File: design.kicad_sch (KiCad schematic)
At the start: 1 part

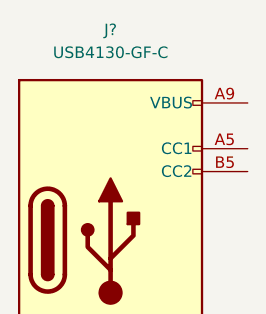
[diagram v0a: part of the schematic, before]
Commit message: annotate + usb connector 3D
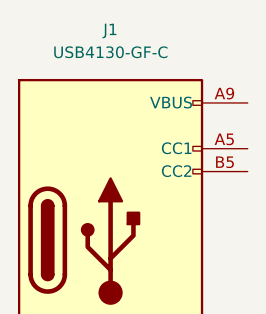
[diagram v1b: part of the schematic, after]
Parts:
- gave numbers to parts that had none: 1
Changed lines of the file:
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@@
   (symbol (lib_id "Connector_custom:USB4130-GF-C") (at 69.088 65.278 0) (unit 1)
     (in_bom yes) (on_board yes) (fields_autoplaced)
-    (property "Reference" "J?" (id 0) (at 69.088 41.91 0))
+    (property "Reference" "J1" (id 0) (at 69.088 41.91 0))
     (property "Value" "USB4130-GF-C" (id 1) (at 69.088 44.45 0))
     (property "Footprint" "Connector_USB_custom:USB_C_Receptacle_GCT_USB4130-GF-C" (id 2) (at 72.898 65.278 0)
@@
   (symbol_instances
     (path "/b1b78902-1557-46e9-9466-76f6cf11f8e2"
-      (reference "J?") (unit 1) (value "USB4130-GF-C") (footprint "Connector_USB_custom:USB_C_Receptacle_GCT_USB4130-GF-C")
+      (reference "J1") (unit 1) (value "USB4130-GF-C") (footprint "Connector_USB_custom:USB_C_Receptacle_GCT_USB4130-GF-C")
     )
   )

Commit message: update template to v0.45
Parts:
- added C?: 100nF, Capacitor_SMD:C_0805_2012Metric, symbol Device:C_Small
- added C?: 10uF, Capacitor_SMD:C_0805_2012Metric, symbol Device:C_Small
- added C?: 0-50pF, Capacitor_SMD:C_0805_2012Metric, symbol Device:C_Small
- added C? (x3): 1uF, Capacitor_SMD:C_0805_2012Metric, symbol Device:C_Small
- added C?: 0.1uF, Capacitor_SMD:C_0805_2012Metric, symbol Device:C_Small
- added D?: D_Small, Diode_SMD:D_SOD-323, symbol Device:D_Small
- added D?: LED, LED_SMD:LED_0603_1608Metric, symbol Device:LED
- added JP?: TOG, Jumper:SolderJumper-2_P1.3mm_Open_RoundedPad1.0x1.5mm, symbol Jumper:Jumper_2_Open
- added JP?: AHLB, Jumper:SolderJumper-2_P1.3mm_Open_RoundedPad1.0x1.5mm, symbol Jumper:Jumper_2_Open
- added R? (x5): 10K, Resistor_SMD:R_0805_2012Metric, symbol Device:R_Small
- added R?: 470, Resistor_SMD:R_0805_2012Metric, symbol Device:R_Small
- added SW?: EN, Button_Switch_SMD:SW_SPST_EVPBF, symbol Switch:SW_Push
- added SW?: IO9, Button_Switch_SMD:SW_SPST_EVPBF, symbol Switch:SW_Push
- added TP? (x3): Vin, TestPoint:TestPoint_Pad_D2.5mm, symbol Connector:TestPoint
- added TP?: touch_point_1, symbol Connector:TestPoint
- added TP?: +3.3V, TestPoint:TestPoint_Pad_D2.5mm, symbol Connector:TestPoint
- added TP?: Vbat, TestPoint:TestPoint_Pad_D2.5mm, symbol Connector:TestPoint
- added TP?: GND, TestPoint:TestPoint_Pad_D2.5mm, symbol Connector:TestPoint
- added U?: TCK108AF,LF, Package_TO_SOT_SMD:SOT-23-5, symbol Power_Management_custom:TCK108AF,LF
- added U?: ESP32-C3-WROOM-02-N4, MCU_Espressif_custom:MODULE_ESP32-C3-WROOM-02-H4, symbol MCU_Espressif_custom:ESP32-C3-WROOM-02-N4
- added U?: TTP223, Package_TO_SOT_SMD:SOT-23-6_Handsoldering, symbol LEDs:TTP223
- added U?: MCP1700-3302E_SOT23, Package_TO_SOT_SMD:SOT-23, symbol Regulator_Linear:MCP1700-3302E_SOT23
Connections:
- new net: C?.1, U?.2 (VO), U?.5 (VIN)
- new net: JP?.1 (A), U?.6 (TOG)
- new net: D?.1 (K), R?.1
- new net +3.3V: C?.1, C?.1, R?.1, R?.1, R?.1, R?.1, TP?.1, U?.1 (3V3), U?.1 (VOUT)
- new net +5V: C?.1, U?.3 (VI)
- new net D+: TP?.1, U?.14 (IO19)
- new net D-: TP?.1, U?.13 (IO18)
- new net EN: C?.1, R?.2, SW?.2, U?.2 (EN)
- new net GND: C?.2, C?.2, C?.2, C?.2, C?.2, C?.2, C?.2, R?.2, R?.2, SW?.1, SW?.1, TP?.1, U?.1 (GND), U?.19 (GND), U?.2 (GND), U?.2 (GND), U?.20 (GND), U?.21 (GND), U?.22 (GND), U?.23 (GND), U?.24 (GND), U?.25 (GND), U?.26 (GND), U?.27 (GND), U?.28 (GND), U?.29 (GND), U?.30 (GND), U?.31 (GND), U?.32 (GND), U?.33 (GND), U?.34 (GND), U?.35 (GND), U?.36 (GND), U?.37 (GND), U?.38 (GND), U?.39 (GND), U?.9 (GND)
- new net IO0: U?.18 (IO0)
- new net IO1: U?.17 (IO1)
- new net IO10: U?.10 (IO10)
- new net IO2: R?.2, U?.16 (IO2)
- new net IO3: U?.15 (IO3)
- new net IO4: U?.3 (IO4)
- new net IO5: D?.2 (A), U?.1 (Q), U?.4 (IO5)
- new net IO6: D?.1 (K), R?.1, U?.3 (Control), U?.5 (IO6)
- new net IO7: D?.2 (A), U?.6 (IO7)
- new net IO8: R?.2, U?.7 (IO8)
- new net IO9: R?.2, SW?.2, U?.8 (IO9)
- new net MCU_RX: U?.11 (RXD)
- new net MCU_TX: U?.12 (TXD)
- new net VCC: C?.1, JP?.2 (B), U?.5 (VCC)
- new net Vbat: TP?.1
- new net Vin: TP?.1
- new net touch_point_1: C?.1, TP?.1, U?.3 (I)
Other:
- note added: "No intenal LDO - feed with fixed valtage between 2-5.5V"
- note added: "TOG: LOW - Direct Mode HIGH - Toggle Mode AHLB: LOW - CMOS active high output HIGH - CMOS active low output"
- note added: "Touch"
- note added: "Touch IC TTP223"
- moved on the sheet: J1

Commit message: Update design.kicad_sch
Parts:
- removed D?: D_Small, Diode_SMD:D_SOD-323, symbol Device:D_Small
- removed JP?: AHLB, Jumper:SolderJumper-2_P1.3mm_Open_RoundedPad1.0x1.5mm, symbol Jumper:Jumper_2_Open
- added JP?: AHLB, symbol Jumper:Jumper_2_Bridged
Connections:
- net IO5: no longer U?.1 (Q)
- net IO6: now also U?.1 (Q)
- net VCC: now also JP?.2 (B)
- net at U?.4 (AHLB): now also JP?.1 (A)
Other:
- moved on the sheet: C?, D?, JP?, R?, SW?, TP?, U?

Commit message: PCB&SCH update
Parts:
- removed TP?: Vin, TestPoint:TestPoint_Pad_D2.5mm, symbol Connector:TestPoint
- removed TP?: Vbat, TestPoint:TestPoint_Pad_D2.5mm, symbol Connector:TestPoint
- added R7, R8: 5.1k, Resistor_SMD:R_0805_2012Metric, symbol Device:R_Small
- added TP4: +BATT, TestPoint:TestPoint_Pad_D2.5mm, symbol Connector:TestPoint
- JP2: renamed from JP?; footprint (none) -> Jumper:SolderJumper-2_P1.3mm_Open_RoundedPad1.0x1.5mm
- TP2: renamed from TP?; value Vin -> D-
- TP3: renamed from TP?; value Vin -> D+
- gave numbers to parts that had none: 24
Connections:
- net VCC is gone; now on net +BATT: C6.1, JP1.2 (B), JP2.2 (B), U4.5 (VCC)
- net +3.3V: now also C2.1, U1.2 (VO); no longer U2.1 (VOUT)
- net GND: now also J1.A12 (GND), J1.B12 (GND), R7.2, R8.2
- net at J1.A5 (CC1): now also R7.1
- net +BATT: now reaches J1.A9 (VBUS), J1.B9 (VBUS)
- net +BATT: now also U2.5 (VIN), TP4.1
- net at J1.B5 (CC2): now also R8.1
- net +5V: no longer names the net of C1.1, U1.3 (VI)
- net +5V: now also U2.1 (VOUT)
- no-connect marks 0 -> 1
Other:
- moved on the sheet: C1, C2, R1, TP5, U1, U2A

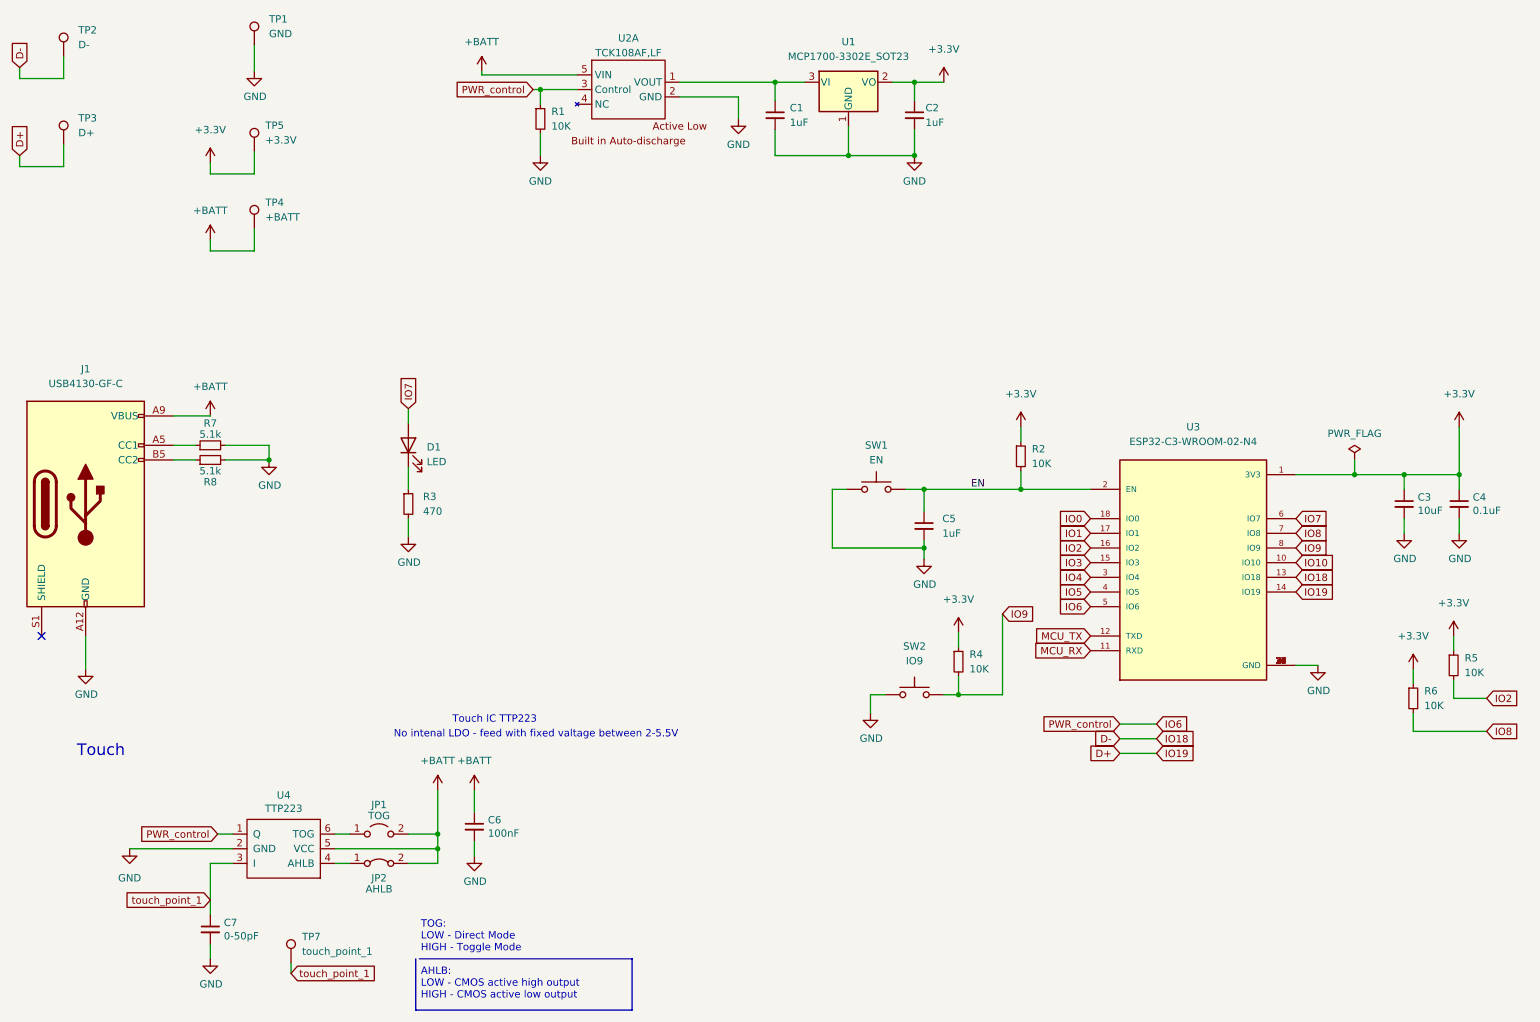
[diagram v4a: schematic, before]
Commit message: SCH handle all ERC error warnings
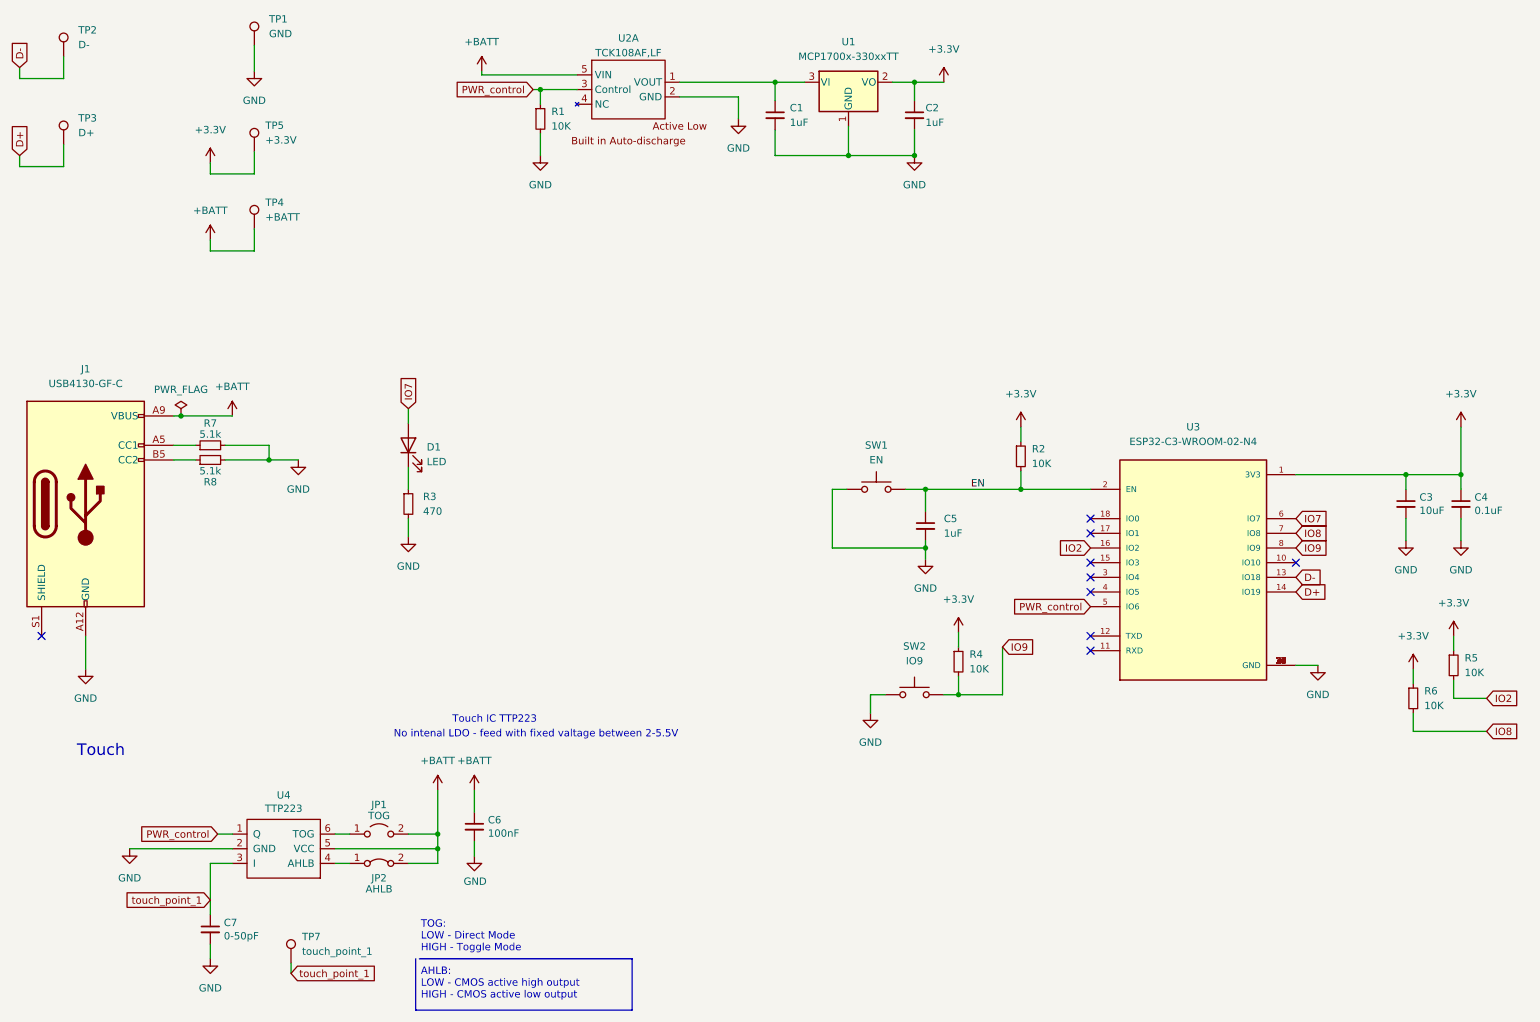
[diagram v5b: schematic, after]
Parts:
- removed U1: MCP1700-3302E_SOT23, Package_TO_SOT_SMD:SOT-23, symbol Regulator_Linear:MCP1700-3302E_SOT23
- added U1: MCP1700x-330xxTT, Package_TO_SOT_SMD:SOT-23, symbol Regulator_Linear:MCP1700x-330xxTT
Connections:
- net +3.3V: now also U1.2 (VO)
- net GND: now also U1.1 (GND)
- net at C1.1, U2.1 (VOUT): now also U1.3 (VI)
- net IO0: no longer names the net of U3.18 (IO0)
- net IO1: no longer names the net of U3.17 (IO1)
- net IO10: no longer names the net of U3.10 (IO10)
- net IO3: no longer names the net of U3.15 (IO3)
- net IO4: no longer names the net of U3.3 (IO4)
- net IO5: no longer names the net of U3.4 (IO5)
- net IO6 renamed PWR_control
- net MCU_RX: no longer names the net of U3.11 (RXD)
- net MCU_TX: no longer names the net of U3.12 (TXD)
- no-connect marks 1 -> 9

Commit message: changes SCH PCB
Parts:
- removed J1: USB4130-GF-C, Connector_USB_custom:USB_C_Receptacle_GCT_USB4130-GF-C, symbol Connector_custom:USB4130-GF-C
- added C8, C9: 1uF, Capacitor_SMD:C_0805_2012Metric, symbol Device:C_Small
- added D2: D_Small, Diode_SMD:D_SOD-323, symbol Device:D_Small
- added J1: HRO_TYPE-C-31-M-12, Connector_USB:USB_C_Receptacle_HRO_TYPE-C-31-M-12, symbol Connector:USB_C_Receptacle
- added J2: SKEDD:490107670612, Connector_custom:WURTH_490107670612, symbol Connector_custom:SKEDD{colon}490107670612
- added J3: Conn_02x03_Odd_Even, symbol Connector_Generic:Conn_02x03_Odd_Even
- added SW3: 5V/3.3V, Button_Switch_SMD:SW_DPDT_CK_JS202011JCQN, symbol Switch:SW_DPDT_x2
- added SW4: VDD/NC, Button_Switch_SMD:SW_DPDT_CK_JS202011JCQN, symbol Switch:SW_DPDT_x2
- added U5: MCP1700x-330xxTT, Package_TO_SOT_SMD:SOT-23, symbol Regulator_Linear:MCP1700x-330xxTT
- SW1, SW2: footprint Button_Switch_SMD:SW_SPST_EVPBF -> Button_Switch_SMD_custom:RKB2
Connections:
- net +3.3V: now also C9.1, J2.5 (VIN), SW3.3 (C), U5.2 (VO)
- net D+: now also J1.A6 (D+), J1.B6 (D+), J3.6 (Pin_6); no longer U3.14 (IO19)
- net D-: now also J1.A7 (D-), J1.B7 (D-), J3.4 (Pin_4); no longer U3.13 (IO18)
- net GND: now also R7.1, R8.1, SW1.2, SW2.2, C8.2, C9.2, J1.A1 (GND), J1.A12 (GND), J1.B1 (GND), J1.B12 (GND), J1.S1 (SHIELD), J2.2 (GND), U5.1 (GND); no longer R7.2, R8.2, SW1.1, SW2.1
- net IO9: now also J2.3 (RX); no longer SW2.2
- net PWR_control: now also D2.1 (K); no longer U4.1 (Q)
- net USB_input: now reaches C1.1, U1.3 (VI), U2.1 (VOUT)
- net EN renamed MCU_EN
- net MCU_EN: now also J2.1 (TX); no longer SW1.2
- new net: SW3.2 (B), SW4.1 (A)
- new net: D2.2 (A), U4.1 (Q)
- new net CC1: J1.A5 (CC1), R8.2
- new net CC2: J1.B5 (CC2), R7.2
- new net Ex_EN: J3.1 (Pin_1), SW1.1
- new net Ex_IO9: J3.3 (Pin_3), SW2.1
- new net MCU_D+: J2.6 (D+/UPDI), U3.14 (IO19)
- new net MCU_D-: J2.4 (D-), U3.13 (IO18)
- new net VBUS: C8.1, J1.A4 (VBUS), J1.A9 (VBUS), J1.B4 (VBUS), J1.B9 (VBUS), SW3.1 (A), U5.3 (VI)
- new net VDD: J3.5 (Pin_5), SW4.2 (B)
- no-connect marks 9 -> 18
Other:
- note added: "LOW - OFF HIGH - ON"
- moved on the sheet: D1, R3, SW1, SW2

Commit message: more update PCB SCH
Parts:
- removed TP2: D-, TestPoint:TestPoint_Pad_D2.5mm, symbol Connector:TestPoint
- removed TP3: D+, TestPoint:TestPoint_Pad_D2.5mm, symbol Connector:TestPoint
- added C10, C11: 1uF, Capacitor_SMD:C_0805_2012Metric, symbol Device:C_Small
- J3: footprint (none) -> Connector_PinHeader_2.54mm:PinHeader_2x03_P2.54mm_Vertical
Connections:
- net +3.3V: no longer C9.1, SW3.3 (C), U5.2 (VO)
- net GND: now also J3.2 (Pin_2), C10.2, C11.2
- net USB_input: now also C10.1, C11.1
- new net +3V3: C9.1, SW3.3 (C), U5.2 (VO)

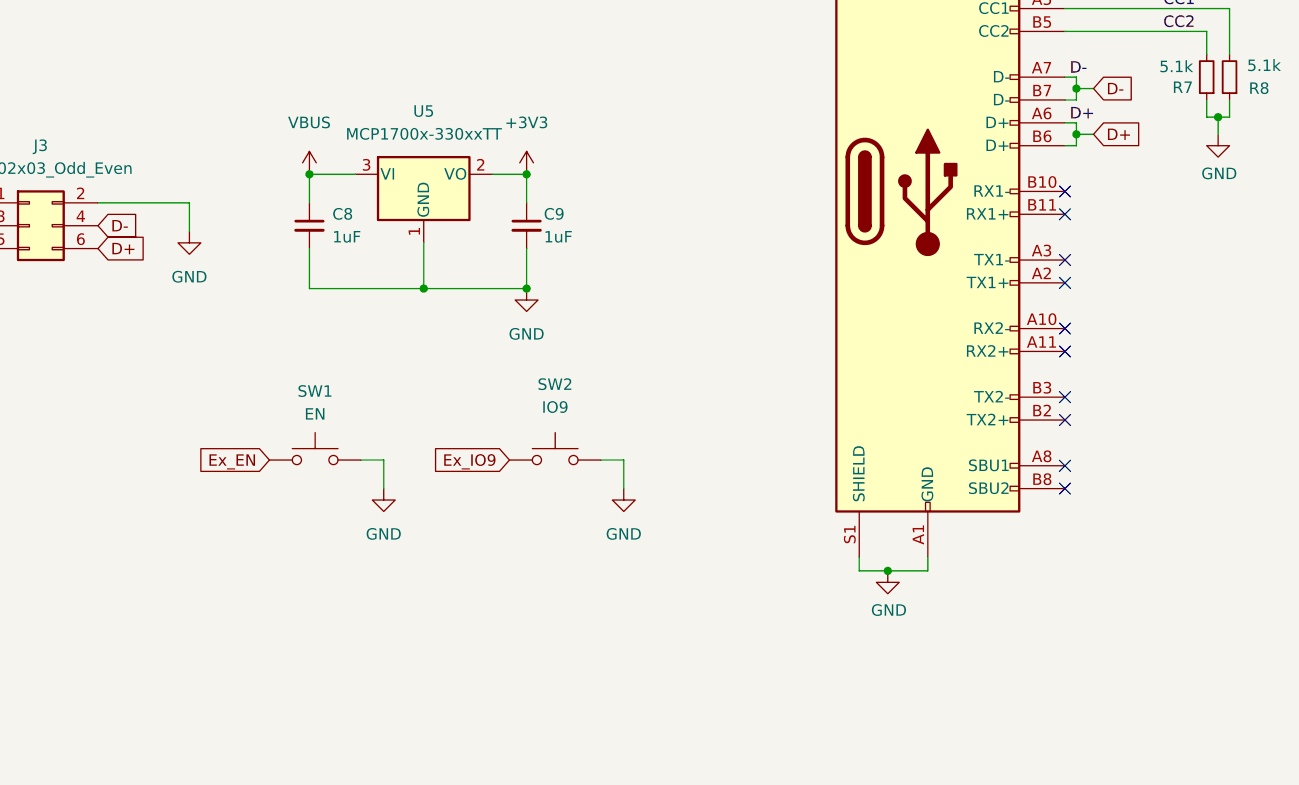
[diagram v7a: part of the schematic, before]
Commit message: put USB section own GND2 signal
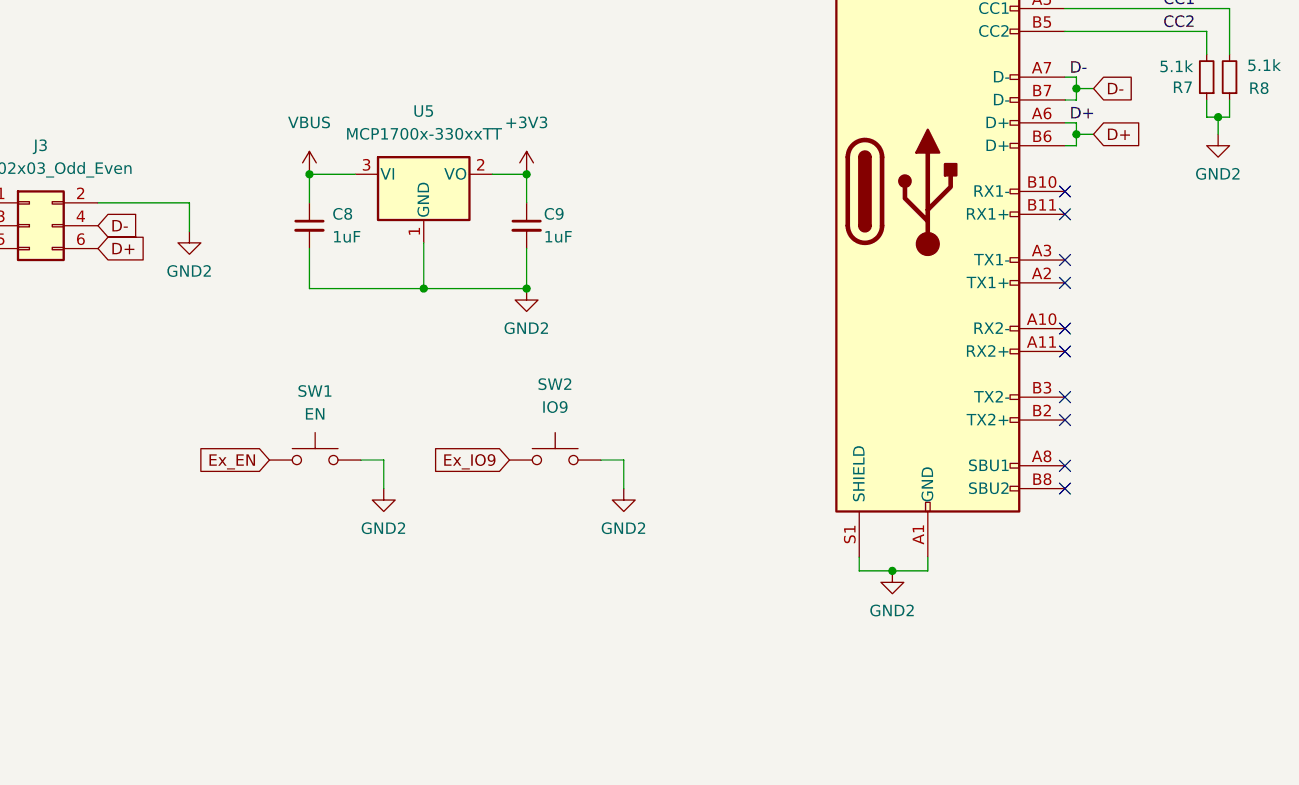
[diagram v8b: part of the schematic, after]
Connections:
- net GND: no longer C8.2, C9.2, J1.A1 (GND), J1.A12 (GND), J1.B1 (GND), J1.B12 (GND), J1.S1 (SHIELD), J3.2 (Pin_2), R7.1, R8.1, SW1.2, SW2.2, U5.1 (GND)
- new net GND2: C8.2, C9.2, J1.A1 (GND), J1.A12 (GND), J1.B1 (GND), J1.B12 (GND), J1.S1 (SHIELD), J3.2 (Pin_2), R7.1, R8.1, SW1.2, SW2.2, U5.1 (GND)
